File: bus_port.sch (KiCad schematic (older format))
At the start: 3 parts

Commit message: Another new board layout. Few tidy ups.
Removed the single step circuit, not worth the board space and headache.
Added legend for the IO slot for easy reference. Still toying where to
put the power LED, annoying me with that resistor. Think I'm happy with
it now. Spaced things out a little to make it easy for manufacture, made
sure no traces are near board edges as much as possible.
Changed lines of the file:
@@
 AR Path="/577F17CE/5797AD5E/5780CE22" Ref="CD1"  Part="1"
 AR Path="/577F17CE/5798778E/5780CE22" Ref="CE1"  Part="1"
-F 0 "CE1" H 3025 4650 50  0000 L CNN
+F 0 "CB1" H 3025 4650 50  0000 L CNN
 F 1 "100n" H 3025 4450 50  0000 L CNN
 F 2 "Capacitors_ThroughHole:C_Rect_L4_W2.5_P2.5" H 3038 4400 50  0001 C CNN
@@
 	3000 4700 3000 4800
 $Comp
-L VCC #PWR040
+L VCC #PWR028
 U 1 1 5780D6F2
 P 3000 4300
-AR Path="/577F17CE/577F1897/5780D6F2" Ref="#PWR040"  Part="1"
+AR Path="/577F17CE/577F1897/5780D6F2" Ref="#PWR028"  Part="1"
 AR Path="/577F17CE/5782F6B6/5780D6F2" Ref="#PWR045"  Part="1"
 AR Path="/577F17CE/5783136E/5780D6F2" Ref="#PWR047"  Part="1"
 AR Path="/577F17CE/57832B70/5780D6F2" Ref="#PWR057"  Part="1"
-AR Path="/577F17CE/57978710/5780D6F2" Ref="#PWR042"  Part="1"
-AR Path="/577F17CE/5797AC61/5780D6F2" Ref="#PWR044"  Part="1"
-AR Path="/577F17CE/5797AD5E/5780D6F2" Ref="#PWR046"  Part="1"
-AR Path="/577F17CE/5798778E/5780D6F2" Ref="#PWR048"  Part="1"
-F 0 "#PWR048" H 3000 4150 50  0001 C CNN
+AR Path="/577F17CE/57978710/5780D6F2" Ref="#PWR030"  Part="1"
+AR Path="/577F17CE/5797AC61/5780D6F2" Ref="#PWR032"  Part="1"
+AR Path="/577F17CE/5797AD5E/5780D6F2" Ref="#PWR034"  Part="1"
+AR Path="/577F17CE/5798778E/5780D6F2" Ref="#PWR036"  Part="1"
+F 0 "#PWR030" H 3000 4150 50  0001 C CNN
 F 1 "VCC" H 3000 4450 50  0000 C CNN
 F 2 "" H 3000 4300 50  0000 C CNN
@@
 $EndComp
 $Comp
-L GND #PWR041
+L GND #PWR029
 U 1 1 5780D706
 P 3000 4800
-AR Path="/577F17CE/577F1897/5780D706" Ref="#PWR041"  Part="1"
+AR Path="/577F17CE/577F1897/5780D706" Ref="#PWR029"  Part="1"
 AR Path="/577F17CE/5782F6B6/5780D706" Ref="#PWR046"  Part="1"
 AR Path="/577F17CE/5783136E/5780D706" Ref="#PWR048"  Part="1"
 AR Path="/577F17CE/57832B70/5780D706" Ref="#PWR058"  Part="1"
-AR Path="/577F17CE/57978710/5780D706" Ref="#PWR043"  Part="1"
-AR Path="/577F17CE/5797AC61/5780D706" Ref="#PWR045"  Part="1"
-AR Path="/577F17CE/5797AD5E/5780D706" Ref="#PWR047"  Part="1"
-AR Path="/577F17CE/5798778E/5780D706" Ref="#PWR049"  Part="1"
-F 0 "#PWR049" H 3000 4550 50  0001 C CNN
+AR Path="/577F17CE/57978710/5780D706" Ref="#PWR031"  Part="1"
+AR Path="/577F17CE/5797AC61/5780D706" Ref="#PWR033"  Part="1"
+AR Path="/577F17CE/5797AD5E/5780D706" Ref="#PWR035"  Part="1"
+AR Path="/577F17CE/5798778E/5780D706" Ref="#PWR037"  Part="1"
+F 0 "#PWR031" H 3000 4550 50  0001 C CNN
 F 1 "GND" H 3000 4650 50  0000 C CNN
 F 2 "" H 3000 4800 50  0000 C CNN
@@
 AR Path="/577F17CE/5797AD5E/579E12E5" Ref="PD1"  Part="1"
 AR Path="/577F17CE/5798778E/579E12E5" Ref="PE1"  Part="1"
-F 0 "PE1" H 4450 6750 50  0000 C CNN
+F 0 "PB1" H 4450 6750 50  0000 C CNN
 F 1 "CONN_01X40" V 4550 6400 50  0001 C CNN
 F 2 "Socket_Strips:Socket_Strip_Straight_1x40" H 4450 4700 50  0001 C CNN
@@
 AR Path="/577F17CE/5797AD5E/579E1380" Ref="PD2"  Part="1"
 AR Path="/577F17CE/5798778E/579E1380" Ref="PE2"  Part="1"
-F 0 "PE2" H 4500 5550 50  0000 C CNN
+F 0 "PB2" H 4500 5550 50  0000 C CNN
 F 1 "CONN_01X12" V 4650 4900 50  0001 C CNN
 F 2 "Socket_Strips:Socket_Strip_Straight_1x12" H 4550 4900 50  0001 C CNN

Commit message: * added USB data signals to first slot * added logo to the top of the board. * added logo PNG files.
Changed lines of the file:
@@
 AR Path="/577F17CE/5797AD5E/5780CE22" Ref="CD1"  Part="1"
 AR Path="/577F17CE/5798778E/5780CE22" Ref="CE1"  Part="1"
-F 0 "CB1" H 3025 4650 50  0000 L CNN
+F 0 "CA1" H 3025 4650 50  0000 L CNN
 F 1 "100n" H 3025 4450 50  0000 L CNN
 F 2 "Capacitors_ThroughHole:C_Rect_L4_W2.5_P2.5" H 3038 4400 50  0001 C CNN
@@
 AR Path="/577F17CE/5797AD5E/5780D6F2" Ref="#PWR034"  Part="1"
 AR Path="/577F17CE/5798778E/5780D6F2" Ref="#PWR036"  Part="1"
-F 0 "#PWR030" H 3000 4150 50  0001 C CNN
+F 0 "#PWR036" H 3000 4150 50  0001 C CNN
 F 1 "VCC" H 3000 4450 50  0000 C CNN
 F 2 "" H 3000 4300 50  0000 C CNN
@@
 AR Path="/577F17CE/5797AD5E/5780D706" Ref="#PWR035"  Part="1"
 AR Path="/577F17CE/5798778E/5780D706" Ref="#PWR037"  Part="1"
-F 0 "#PWR031" H 3000 4550 50  0001 C CNN
+F 0 "#PWR037" H 3000 4550 50  0001 C CNN
 F 1 "GND" H 3000 4650 50  0000 C CNN
 F 2 "" H 3000 4800 50  0000 C CNN
@@
 AR Path="/577F17CE/5797AD5E/579E12E5" Ref="PD1"  Part="1"
 AR Path="/577F17CE/5798778E/579E12E5" Ref="PE1"  Part="1"
-F 0 "PB1" H 4450 6750 50  0000 C CNN
+F 0 "PA1" H 4450 6750 50  0000 C CNN
 F 1 "CONN_01X40" V 4550 6400 50  0001 C CNN
 F 2 "Socket_Strips:Socket_Strip_Straight_1x40" H 4450 4700 50  0001 C CNN
@@
 AR Path="/577F17CE/5797AD5E/579E1380" Ref="PD2"  Part="1"
 AR Path="/577F17CE/5798778E/579E1380" Ref="PE2"  Part="1"
-F 0 "PB2" H 4500 5550 50  0000 C CNN
+F 0 "PA2" H 4500 5550 50  0000 C CNN
 F 1 "CONN_01X12" V 4650 4900 50  0001 C CNN
 F 2 "Socket_Strips:Socket_Strip_Straight_1x12" H 4550 4900 50  0001 C CNN

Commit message: * Replaced one card slot with an updated expansion connector. * Replaced '138 with GAL. * Implemented interrupt priority lines IEI/IEO. * Replaced discrete oscillator with 14/8 pin DIP oscillator block.
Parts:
- removed PA2: CONN_01X12, Socket_Strips:Socket_Strip_Straight_1x12, symbol CONN_01X12
- added PA2: CONN_01X10, symbol CONN_01X10
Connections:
- net labels added: IEI, IEO, ~IOSEL0
- net labels removed: ~IOSEL4, ~IOSEL5, ~IOSEL6, ~IOSEL7, ~IOSEL8
- wire segments 56 -> 54
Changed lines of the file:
@@
 LIBS:6850
 LIBS:nrc2016
+LIBS:atf16v8cv
+LIBS:62256
 LIBS:z80-cache
 EELAYER 25 0
@@
 $Descr A4 11693 8268
 encoding utf-8
-Sheet 8 8
+Sheet 7 8
 Title ""
 Date ""
@@
 AR Path="/577F17CE/5797AD5E/5780CE22" Ref="CD1"  Part="1"
 AR Path="/577F17CE/5798778E/5780CE22" Ref="CE1"  Part="1"
-F 0 "CA1" H 3025 4650 50  0000 L CNN
+F 0 "CD1" H 3025 4650 50  0000 L CNN
 F 1 "100n" H 3025 4450 50  0000 L CNN
 F 2 "Capacitors_ThroughHole:C_Rect_L4_W2.5_P2.5" H 3038 4400 50  0001 C CNN
@@
 	3000 4700 3000 4800
 $Comp
-L VCC #PWR028
+L VCC #PWR29
 U 1 1 5780D6F2
 P 3000 4300
-AR Path="/577F17CE/577F1897/5780D6F2" Ref="#PWR028"  Part="1"
+AR Path="/577F17CE/577F1897/5780D6F2" Ref="#PWR29"  Part="1"
 AR Path="/577F17CE/5782F6B6/5780D6F2" Ref="#PWR045"  Part="1"
 AR Path="/577F17CE/5783136E/5780D6F2" Ref="#PWR047"  Part="1"
 AR Path="/577F17CE/57832B70/5780D6F2" Ref="#PWR057"  Part="1"
-AR Path="/577F17CE/57978710/5780D6F2" Ref="#PWR030"  Part="1"
-AR Path="/577F17CE/5797AC61/5780D6F2" Ref="#PWR032"  Part="1"
-AR Path="/577F17CE/5797AD5E/5780D6F2" Ref="#PWR034"  Part="1"
+AR Path="/577F17CE/57978710/5780D6F2" Ref="#PWR31"  Part="1"
+AR Path="/577F17CE/5797AC61/5780D6F2" Ref="#PWR33"  Part="1"
+AR Path="/577F17CE/5797AD5E/5780D6F2" Ref="#PWR35"  Part="1"
 AR Path="/577F17CE/5798778E/5780D6F2" Ref="#PWR036"  Part="1"
-F 0 "#PWR036" H 3000 4150 50  0001 C CNN
+F 0 "#PWR35" H 3000 4150 50  0001 C CNN
 F 1 "VCC" H 3000 4450 50  0000 C CNN
 F 2 "" H 3000 4300 50  0000 C CNN
@@
 $EndComp
 $Comp
-L GND #PWR029
+L GND #PWR30
 U 1 1 5780D706
 P 3000 4800
-AR Path="/577F17CE/577F1897/5780D706" Ref="#PWR029"  Part="1"
+AR Path="/577F17CE/577F1897/5780D706" Ref="#PWR30"  Part="1"
 AR Path="/577F17CE/5782F6B6/5780D706" Ref="#PWR046"  Part="1"
 AR Path="/577F17CE/5783136E/5780D706" Ref="#PWR048"  Part="1"
 AR Path="/577F17CE/57832B70/5780D706" Ref="#PWR058"  Part="1"
-AR Path="/577F17CE/57978710/5780D706" Ref="#PWR031"  Part="1"
-AR Path="/577F17CE/5797AC61/5780D706" Ref="#PWR033"  Part="1"
-AR Path="/577F17CE/5797AD5E/5780D706" Ref="#PWR035"  Part="1"
+AR Path="/577F17CE/57978710/5780D706" Ref="#PWR32"  Part="1"
+AR Path="/577F17CE/5797AC61/5780D706" Ref="#PWR34"  Part="1"
+AR Path="/577F17CE/5797AD5E/5780D706" Ref="#PWR36"  Part="1"
 AR Path="/577F17CE/5798778E/5780D706" Ref="#PWR037"  Part="1"
-F 0 "#PWR037" H 3000 4550 50  0001 C CNN
+F 0 "#PWR36" H 3000 4550 50  0001 C CNN
 F 1 "GND" H 3000 4650 50  0000 C CNN
 F 2 "" H 3000 4800 50  0000 C CNN
@@
 	3900 6050 4250 6050
 Wire Wire Line
-	5100 4350 4750 4350
-Wire Wire Line
-	5100 4450 4750 4450
-Wire Wire Line
 	3900 5150 4250 5150
 Wire Wire Line
@@
 Wire Wire Line
 	4250 4550 3900 4550
-Text HLabel 5100 5050 2    60   Output ~ 0
+Text HLabel 5100 4850 2    60   Output ~ 0
 ~NMI
 Wire Wire Line
@@
 Wire Wire Line
 	4750 4850 5100 4850
-Wire Wire Line
-	4750 4950 5100 4950
-Wire Wire Line
-	4750 5050 5100 5050
 Text HLabel 3900 4650 0    60   Input ~ 0
 ~RESET
@@
 Text HLabel 3900 5150 0    60   Output ~ 0
 ~RD
-Text HLabel 5100 4850 2    60   Output ~ 0
+Text HLabel 5100 4650 2    60   Output ~ 0
 ~WAIT
-Text HLabel 5100 4750 2    60   Output ~ 0
+Text HLabel 5100 4550 2    60   Output ~ 0
 ~BUSRQ
+Text HLabel 5100 4750 2    60   Input ~ 0
+~BUSACK
+Wire Wire Line
+	4750 4950 5100 4950
+Wire Wire Line
+	4750 5050 5100 5050
+Wire Wire Line
+	4750 5150 5100 5150
+Wire Wire Line
+	4750 5250 5100 5250
 Text HLabel 5100 4950 2    60   Input ~ 0
-~BUSACK
-Wire Wire Line
-	4750 5150 5100 5150
-Wire Wire Line
-	4750 5250 5100 5250
-Wire Wire Line
-	4750 5350 5100 5350
-Wire Wire Line
-	4750 5450 5100 5450
-Text HLabel 5100 4350 2    60   Input ~ 0
+~IOSEL0
+Text HLabel 5100 5050 2    60   Input ~ 0
 ~IOSEL1
-Text HLabel 5100 4450 2    60   Input ~ 0
+Text HLabel 5100 5150 2    60   Input ~ 0
 ~IOSEL2
-Text HLabel 5100 4550 2    60   Input ~ 0
+Text HLabel 5100 5250 2    60   Input ~ 0
 ~IOSEL3
-Text HLabel 5100 4650 2    60   Input ~ 0
-~IOSEL4
-Text HLabel 5100 5150 2    60   Input ~ 0
-~IOSEL5
-Text HLabel 5100 5250 2    60   Input ~ 0
-~IOSEL6
-Text HLabel 5100 5350 2    60   Input ~ 0
-~IOSEL7
-Text HLabel 5100 5450 2    60   Input ~ 0
-~IOSEL8
 $Comp
 L CONN_01X40 PA1
@@
 AR Path="/577F17CE/5797AD5E/579E12E5" Ref="PD1"  Part="1"
 AR Path="/577F17CE/5798778E/579E12E5" Ref="PE1"  Part="1"
-F 0 "PA1" H 4450 6750 50  0000 C CNN
+F 0 "PD1" H 4450 6750 50  0000 C CNN
 F 1 "CONN_01X40" V 4550 6400 50  0001 C CNN
 F 2 "Socket_Strips:Socket_Strip_Straight_1x40" H 4450 4700 50  0001 C CNN
@@
 $EndComp
 $Comp
-L CONN_01X12 PA2
-U 1 1 579E1380
-P 4550 4900
-AR Path="/577F17CE/577F1897/579E1380" Ref="PA2"  Part="1"
-AR Path="/577F17CE/57978710/579E1380" Ref="PB2"  Part="1"
-AR Path="/577F17CE/5797AC61/579E1380" Ref="PC2"  Part="1"
-AR Path="/577F17CE/5797AD5E/579E1380" Ref="PD2"  Part="1"
-AR Path="/577F17CE/5798778E/579E1380" Ref="PE2"  Part="1"
-F 0 "PA2" H 4500 5550 50  0000 C CNN
-F 1 "CONN_01X12" V 4650 4900 50  0001 C CNN
-F 2 "Socket_Strips:Socket_Strip_Straight_1x12" H 4550 4900 50  0001 C CNN
-F 3 "" H 4550 4900 50  0000 C CNN
-	1    4550 4900
+L CONN_01X10 PA2
+U 1 1 57B9EC3D
+P 4550 5000
+AR Path="/577F17CE/577F1897/57B9EC3D" Ref="PA2"  Part="1"
+AR Path="/577F17CE/57978710/57B9EC3D" Ref="PB2"  Part="1"
+AR Path="/577F17CE/5797AC61/57B9EC3D" Ref="PC2"  Part="1"
+AR Path="/577F17CE/5797AD5E/57B9EC3D" Ref="PD2"  Part="1"
+F 0 "PD2" H 4500 5550 50  0000 C CNN
+F 1 "CONN_01X10" V 4650 5000 50  0001 C CNN
+F 2 "" H 4550 5000 50  0000 C CNN
+F 3 "" H 4550 5000 50  0000 C CNN
+	1    4550 5000
 	-1   0    0    -1
 $EndComp
+Text HLabel 5100 5350 2    60   Input ~ 0
+IEI
+Wire Wire Line
+	5100 5350 4750 5350
+Text HLabel 5100 5450 2    60   Output ~ 0
+IEO
+Wire Wire Line
+	5100 5450 4750 5450
 $EndSCHEMATC

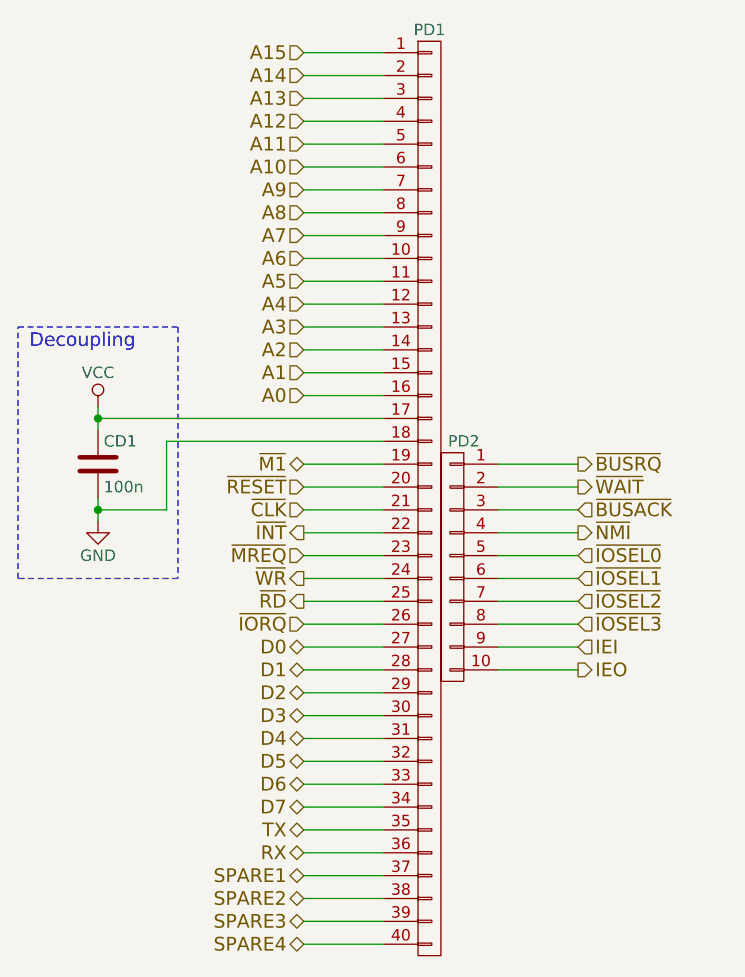
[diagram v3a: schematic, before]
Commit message: Fixed schema DRC errors
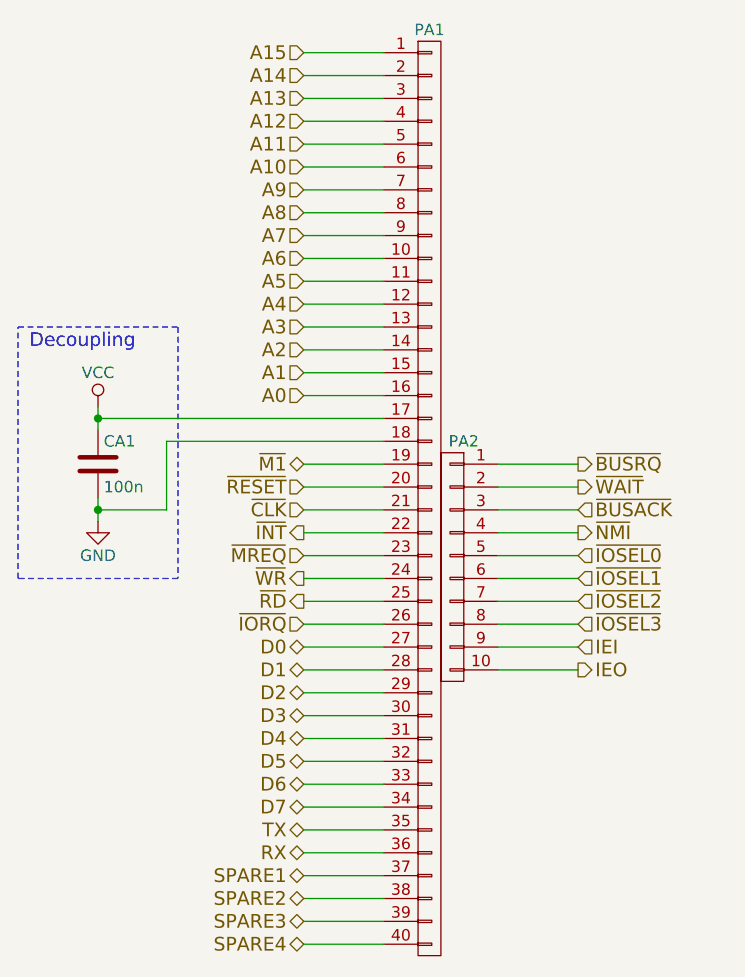
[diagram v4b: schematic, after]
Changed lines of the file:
@@
 $Descr A4 11693 8268
 encoding utf-8
-Sheet 7 8
+Sheet 4 8
 Title ""
 Date ""
@@
 AR Path="/577F17CE/5797AD5E/5780CE22" Ref="CD1"  Part="1"
 AR Path="/577F17CE/5798778E/5780CE22" Ref="CE1"  Part="1"
-F 0 "CD1" H 3025 4650 50  0000 L CNN
+F 0 "CA1" H 3025 4650 50  0000 L CNN
 F 1 "100n" H 3025 4450 50  0000 L CNN
 F 2 "Capacitors_ThroughHole:C_Rect_L4_W2.5_P2.5" H 3038 4400 50  0001 C CNN
@@
 	3000 4700 3000 4800
 $Comp
-L VCC #PWR29
+L VCC #PWR025
 U 1 1 5780D6F2
 P 3000 4300
-AR Path="/577F17CE/577F1897/5780D6F2" Ref="#PWR29"  Part="1"
+AR Path="/577F17CE/577F1897/5780D6F2" Ref="#PWR025"  Part="1"
 AR Path="/577F17CE/5782F6B6/5780D6F2" Ref="#PWR045"  Part="1"
 AR Path="/577F17CE/5783136E/5780D6F2" Ref="#PWR047"  Part="1"
 AR Path="/577F17CE/57832B70/5780D6F2" Ref="#PWR057"  Part="1"
-AR Path="/577F17CE/57978710/5780D6F2" Ref="#PWR31"  Part="1"
-AR Path="/577F17CE/5797AC61/5780D6F2" Ref="#PWR33"  Part="1"
-AR Path="/577F17CE/5797AD5E/5780D6F2" Ref="#PWR35"  Part="1"
+AR Path="/577F17CE/57978710/5780D6F2" Ref="#PWR027"  Part="1"
+AR Path="/577F17CE/5797AC61/5780D6F2" Ref="#PWR029"  Part="1"
+AR Path="/577F17CE/5797AD5E/5780D6F2" Ref="#PWR031"  Part="1"
 AR Path="/577F17CE/5798778E/5780D6F2" Ref="#PWR036"  Part="1"
-F 0 "#PWR35" H 3000 4150 50  0001 C CNN
+F 0 "#PWR031" H 3000 4150 50  0001 C CNN
 F 1 "VCC" H 3000 4450 50  0000 C CNN
 F 2 "" H 3000 4300 50  0000 C CNN
@@
 $EndComp
 $Comp
-L GND #PWR30
+L GND #PWR026
 U 1 1 5780D706
 P 3000 4800
-AR Path="/577F17CE/577F1897/5780D706" Ref="#PWR30"  Part="1"
+AR Path="/577F17CE/577F1897/5780D706" Ref="#PWR026"  Part="1"
 AR Path="/577F17CE/5782F6B6/5780D706" Ref="#PWR046"  Part="1"
 AR Path="/577F17CE/5783136E/5780D706" Ref="#PWR048"  Part="1"
 AR Path="/577F17CE/57832B70/5780D706" Ref="#PWR058"  Part="1"
-AR Path="/577F17CE/57978710/5780D706" Ref="#PWR32"  Part="1"
-AR Path="/577F17CE/5797AC61/5780D706" Ref="#PWR34"  Part="1"
-AR Path="/577F17CE/5797AD5E/5780D706" Ref="#PWR36"  Part="1"
+AR Path="/577F17CE/57978710/5780D706" Ref="#PWR028"  Part="1"
+AR Path="/577F17CE/5797AC61/5780D706" Ref="#PWR030"  Part="1"
+AR Path="/577F17CE/5797AD5E/5780D706" Ref="#PWR032"  Part="1"
 AR Path="/577F17CE/5798778E/5780D706" Ref="#PWR037"  Part="1"
-F 0 "#PWR36" H 3000 4550 50  0001 C CNN
+F 0 "#PWR032" H 3000 4550 50  0001 C CNN
 F 1 "GND" H 3000 4650 50  0000 C CNN
 F 2 "" H 3000 4800 50  0000 C CNN
@@
 AR Path="/577F17CE/5797AD5E/579E12E5" Ref="PD1"  Part="1"
 AR Path="/577F17CE/5798778E/579E12E5" Ref="PE1"  Part="1"
-F 0 "PD1" H 4450 6750 50  0000 C CNN
+F 0 "PA1" H 4450 6750 50  0000 C CNN
 F 1 "CONN_01X40" V 4550 6400 50  0001 C CNN
 F 2 "Socket_Strips:Socket_Strip_Straight_1x40" H 4450 4700 50  0001 C CNN
@@
 AR Path="/577F17CE/5797AC61/57B9EC3D" Ref="PC2"  Part="1"
 AR Path="/577F17CE/5797AD5E/57B9EC3D" Ref="PD2"  Part="1"
-F 0 "PD2" H 4500 5550 50  0000 C CNN
+F 0 "PA2" H 4500 5550 50  0000 C CNN
 F 1 "CONN_01X10" V 4650 5000 50  0001 C CNN
 F 2 "" H 4550 5000 50  0000 C CNN
@@
 Text HLabel 5100 5350 2    60   Input ~ 0
 IEI
-Wire Wire Line
-	5100 5350 4750 5350
 Text HLabel 5100 5450 2    60   Output ~ 0
 IEO
 Wire Wire Line
-	5100 5450 4750 5450
+	4750 5350 5100 5350
+Wire Wire Line
+	4750 5450 5100 5450
 $EndSCHEMATC

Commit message: Added new expansion and GAL to layout.
Haven't routed the osc. or the reset.
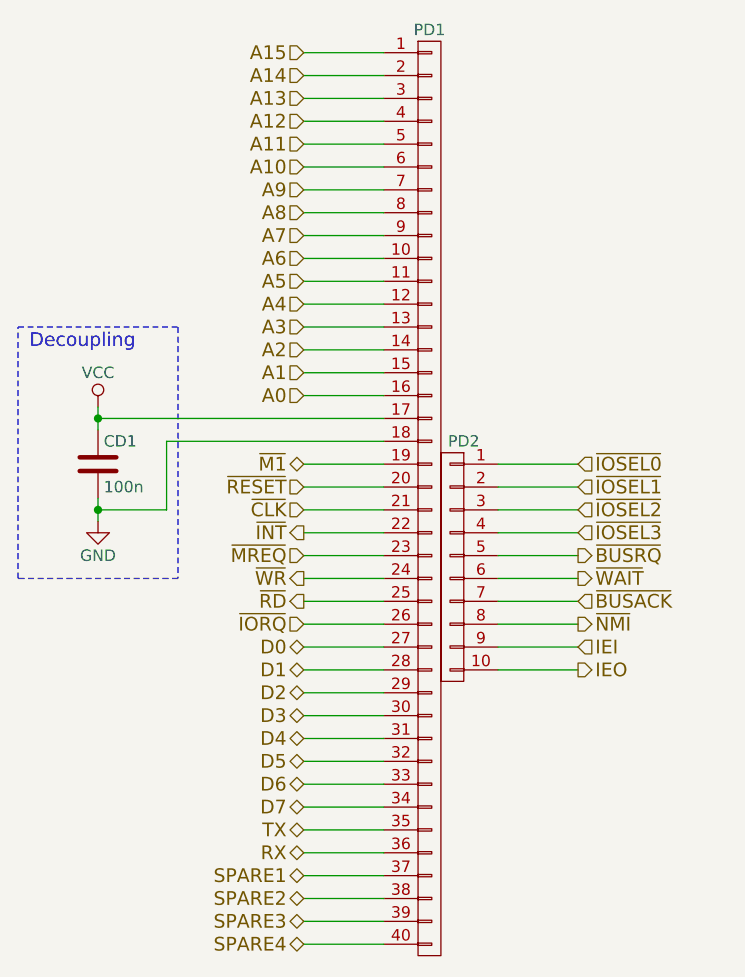
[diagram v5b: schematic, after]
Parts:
- PA2: footprint (none) -> Socket_Strips:Socket_Strip_Straight_1x10
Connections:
- net ~BUSACK: now also PA2.7 (P7); no longer PA2.3 (P3)
- net ~BUSRQ: now also PA2.5 (P5); no longer PA2.1 (P1)
- net ~IOSEL0: now also PA2.1 (P1); no longer PA2.5 (P5)
- net ~IOSEL1: now also PA2.2 (P2); no longer PA2.6 (P6)
- net ~IOSEL2: now also PA2.3 (P3); no longer PA2.7 (P7)
- net ~IOSEL3: now also PA2.4 (P4); no longer PA2.8 (P8)
- net ~NMI: now also PA2.8 (P8); no longer PA2.4 (P4)
- net ~WAIT: now also PA2.6 (P6); no longer PA2.2 (P2)
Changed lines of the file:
@@
 AR Path="/577F17CE/5797AD5E/5780CE22" Ref="CD1"  Part="1"
 AR Path="/577F17CE/5798778E/5780CE22" Ref="CE1"  Part="1"
-F 0 "CA1" H 3025 4650 50  0000 L CNN
+F 0 "CD1" H 3025 4650 50  0000 L CNN
 F 1 "100n" H 3025 4450 50  0000 L CNN
 F 2 "Capacitors_ThroughHole:C_Rect_L4_W2.5_P2.5" H 3038 4400 50  0001 C CNN
@@
 Wire Wire Line
 	4250 4550 3900 4550
-Text HLabel 5100 4850 2    60   Output ~ 0
+Text HLabel 5100 5250 2    60   Output ~ 0
 ~NMI
 Wire Wire Line
@@
 Text HLabel 3900 5150 0    60   Output ~ 0
 ~RD
-Text HLabel 5100 4650 2    60   Output ~ 0
+Text HLabel 5100 5050 2    60   Output ~ 0
 ~WAIT
-Text HLabel 5100 4550 2    60   Output ~ 0
+Text HLabel 5100 4950 2    60   Output ~ 0
 ~BUSRQ
+Text HLabel 5100 5150 2    60   Input ~ 0
+~BUSACK
+Wire Wire Line
+	4750 4950 5100 4950
+Wire Wire Line
+	4750 5050 5100 5050
+Wire Wire Line
+	4750 5150 5100 5150
+Wire Wire Line
+	4750 5250 5100 5250
+Text HLabel 5100 4550 2    60   Input ~ 0
+~IOSEL0
+Text HLabel 5100 4650 2    60   Input ~ 0
+~IOSEL1
 Text HLabel 5100 4750 2    60   Input ~ 0
-~BUSACK
-Wire Wire Line
-	4750 4950 5100 4950
-Wire Wire Line
-	4750 5050 5100 5050
-Wire Wire Line
-	4750 5150 5100 5150
-Wire Wire Line
-	4750 5250 5100 5250
-Text HLabel 5100 4950 2    60   Input ~ 0
-~IOSEL0
-Text HLabel 5100 5050 2    60   Input ~ 0
-~IOSEL1
-Text HLabel 5100 5150 2    60   Input ~ 0
 ~IOSEL2
-Text HLabel 5100 5250 2    60   Input ~ 0
+Text HLabel 5100 4850 2    60   Input ~ 0
 ~IOSEL3
 $Comp
@@
 AR Path="/577F17CE/5797AD5E/579E12E5" Ref="PD1"  Part="1"
 AR Path="/577F17CE/5798778E/579E12E5" Ref="PE1"  Part="1"
-F 0 "PA1" H 4450 6750 50  0000 C CNN
+F 0 "PD1" H 4450 6750 50  0000 C CNN
 F 1 "CONN_01X40" V 4550 6400 50  0001 C CNN
 F 2 "Socket_Strips:Socket_Strip_Straight_1x40" H 4450 4700 50  0001 C CNN
@@
 AR Path="/577F17CE/5797AC61/57B9EC3D" Ref="PC2"  Part="1"
 AR Path="/577F17CE/5797AD5E/57B9EC3D" Ref="PD2"  Part="1"
-F 0 "PA2" H 4500 5550 50  0000 C CNN
+F 0 "PD2" H 4500 5550 50  0000 C CNN
 F 1 "CONN_01X10" V 4650 5000 50  0001 C CNN
-F 2 "" H 4550 5000 50  0000 C CNN
+F 2 "Socket_Strips:Socket_Strip_Straight_1x10" H 4550 5000 50  0001 C CNN
 F 3 "" H 4550 5000 50  0000 C CNN
 	1    4550 5000
